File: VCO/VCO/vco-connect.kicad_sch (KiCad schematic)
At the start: 6 parts, among them J12 Conn_01x11, J13 Conn_01x06, J14 Conn_01x11, J15 Conn_01x06, J16 Conn_01x02, J17 Conn_01x02

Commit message: misc
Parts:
- added J13: Conn_02x05_Odd_Even, Connector_PinHeader_2.54mm:PinHeader_2x05_P2.54mm_Vertical, symbol Connector_Generic:Conn_02x05_Odd_Even
- renumbered J12 to J14, J13 to J15, J14 to J17, J15 to J18, J17 to J19
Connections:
- net +12V: now also J13.10 (Pin_10), J13.9 (Pin_9)
- net -12V: now also J13.1 (Pin_1), J13.2 (Pin_2)
- net GND: now also J13.3 (Pin_3), J13.4 (Pin_4), J13.5 (Pin_5), J13.6 (Pin_6), J13.7 (Pin_7), J13.8 (Pin_8)

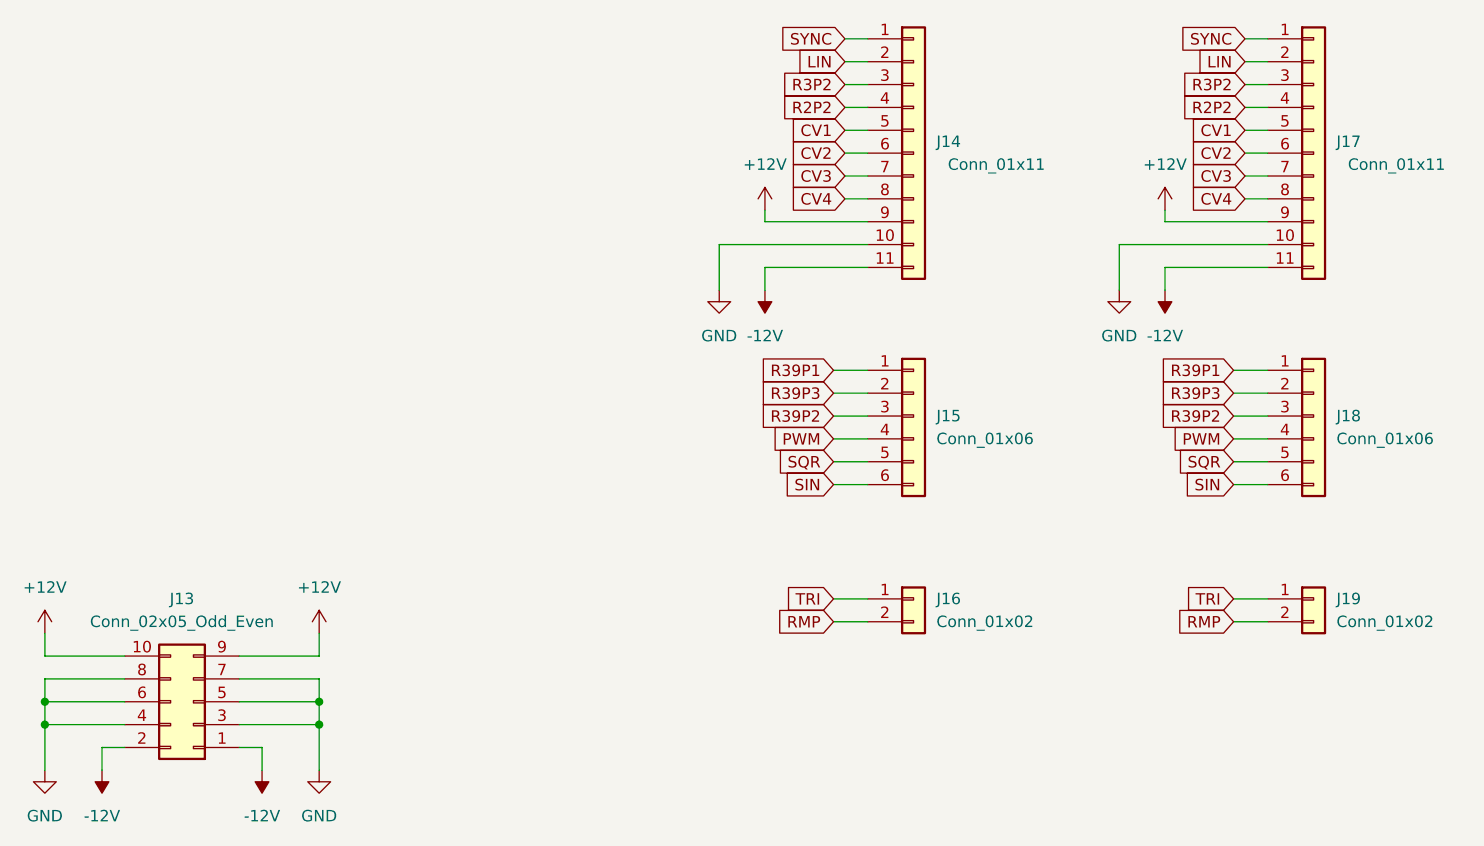
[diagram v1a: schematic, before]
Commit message: split VCO controls plane in separate project
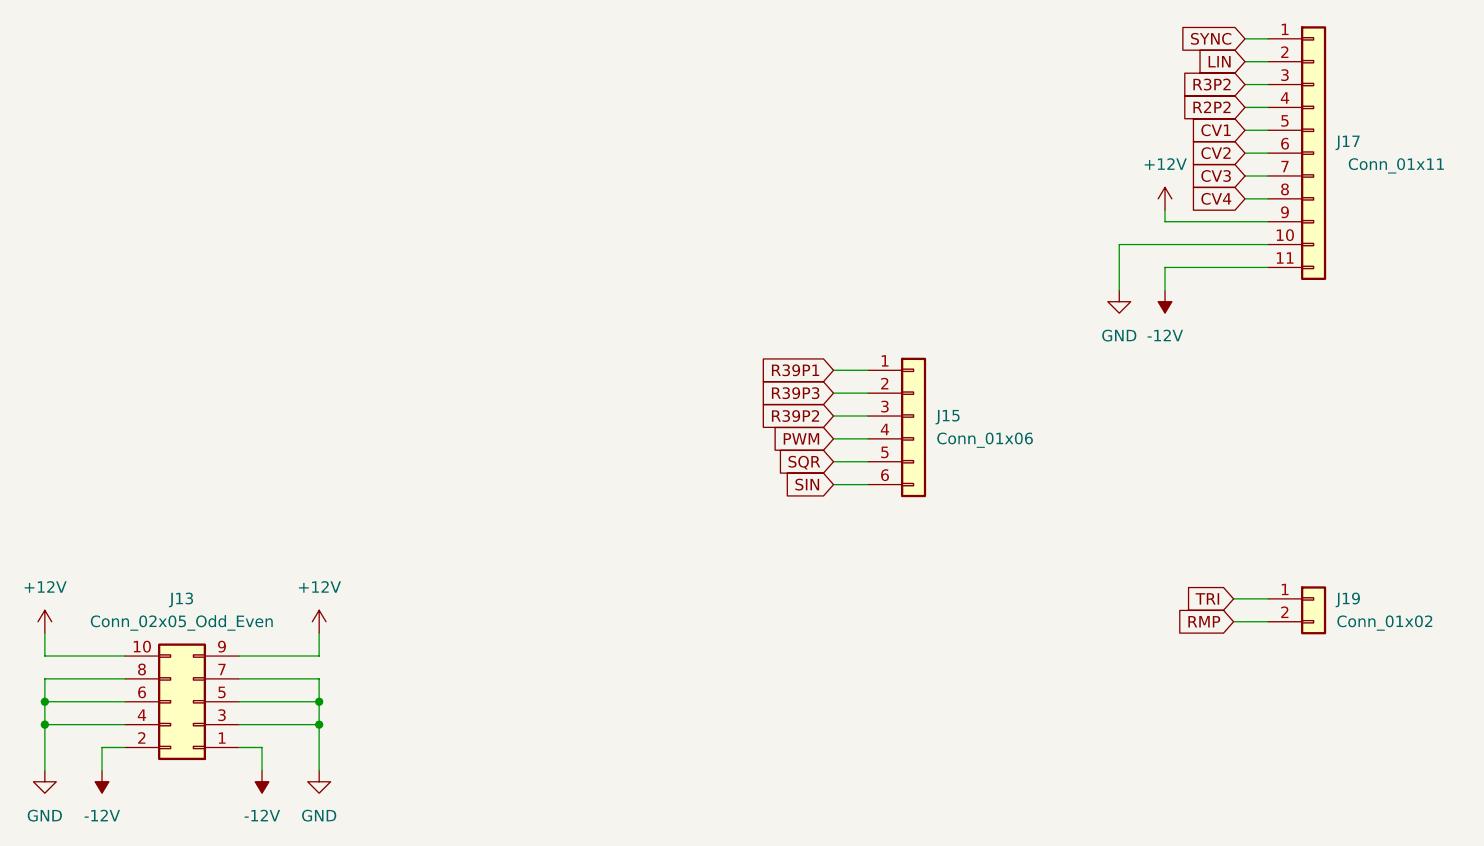
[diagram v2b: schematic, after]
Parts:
- removed J14: Conn_01x11, Connector_PinHeader_2.54mm:PinHeader_1x11_P2.54mm_Vertical, symbol Connector_Generic:Conn_01x11
- removed J16: Conn_01x02, Connector_PinHeader_2.54mm:PinHeader_1x02_P2.54mm_Vertical, symbol Connector_Generic:Conn_01x02
- removed J18: Conn_01x06, Connector_PinHeader_2.54mm:PinHeader_1x06_P2.54mm_Vertical, symbol Connector_Generic:Conn_01x06
